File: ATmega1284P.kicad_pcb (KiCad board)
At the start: 2 copper layers, 45.7 x 22.9 mm, 23 parts, among them J1 Conn_02x03_Odd_Even, J2 Conn_01x06_Male, J3 Conn_01x17_Male, J4 Conn_01x17_Male, J5 Conn_01x01_Male, SW1 SW_Push, U1 ATmega1284P-A, Y1 16MHz

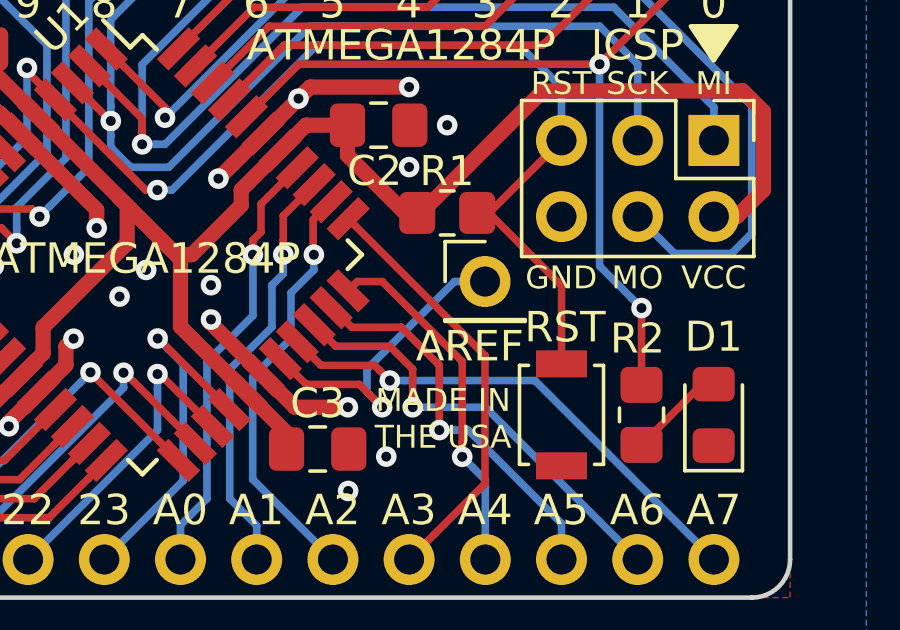
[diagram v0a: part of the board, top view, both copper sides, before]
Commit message: KiCad Files
Aligned AREF pin to be 0.1" offset from the ICSP
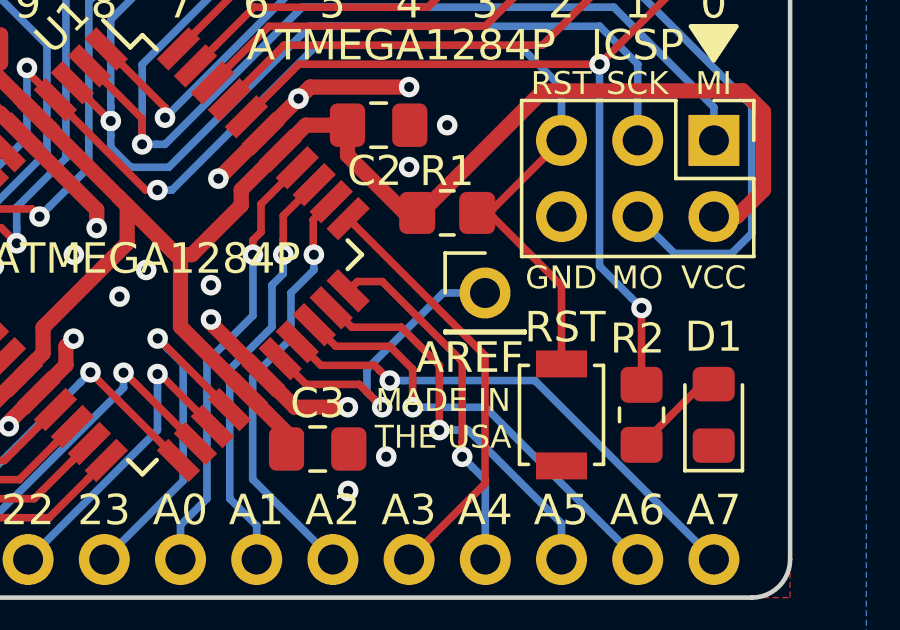
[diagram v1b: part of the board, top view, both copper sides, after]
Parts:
- moved J5 0.38 mm to (151.1, 94.4)
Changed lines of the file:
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@@
   (general
     (thickness 1.6)
-    (drawings 107)
+    (drawings 109)
     (tracks 409)
     (zones 0)
@@
   )
   (module Connector_PinHeader_2.54mm:PinHeader_1x01_P2.54mm_Vertical (layer F.Cu)
-    (at 151.13 93.98)
+    (at 151.13 94.361)
     (descr "Through hole straight pin header, 1x01, 2.54mm pitch, single row")
     (tags "Through hole pin header THT 1x01 2.54mm single row")
@@
       ))
   )
-  (gr_text AREF (at 150.622 96.139) (layer F.SilkS)
+  (gr_line (start 153.67 94.361) (end 151.13 94.361) (layer Dwgs.User) (width 0.1524))
+  (gr_line (start 153.67 91.821) (end 153.67 94.361) (layer Dwgs.User) (width 0.1524))
+  (gr_text AREF (at 150.622 96.52) (layer F.SilkS)
     (effects (font (size 1.016 1.016) (thickness 0.1524)))
   )
@@
   (segment (start 144.304926 96.550905) (end 145.163021 97.409) (width 0.254) (layer F.Cu) (net 41))
   (segment (start 145.163021 97.409) (end 146.939 97.409) (width 0.254) (layer F.Cu) (net 41))
-  (segment (start 150.114 93.98) (end 151.13 93.98) (width 0.254) (layer B.Cu) (net 41))
+  (segment (start 149.733 94.361) (end 151.13 94.361) (width 0.254) (layer B.Cu) (net 41))
+  (segment (start 147.193 96.901) (end 149.733 94.361) (width 0.254) (layer B.Cu) (net 41))
   (segment (start 147.701 98.171) (end 147.193 97.663) (width 0.254) (layer B.Cu) (net 41))
-  (segment (start 147.193 96.901) (end 150.114 93.98) (width 0.254) (layer B.Cu) (net 41))
   (segment (start 147.193 97.663) (end 147.193 96.901) (width 0.254) (layer B.Cu) (net 41))
   (zone (net 2) (net_name GND) (layer F.Cu) (hatch edge 0.508)

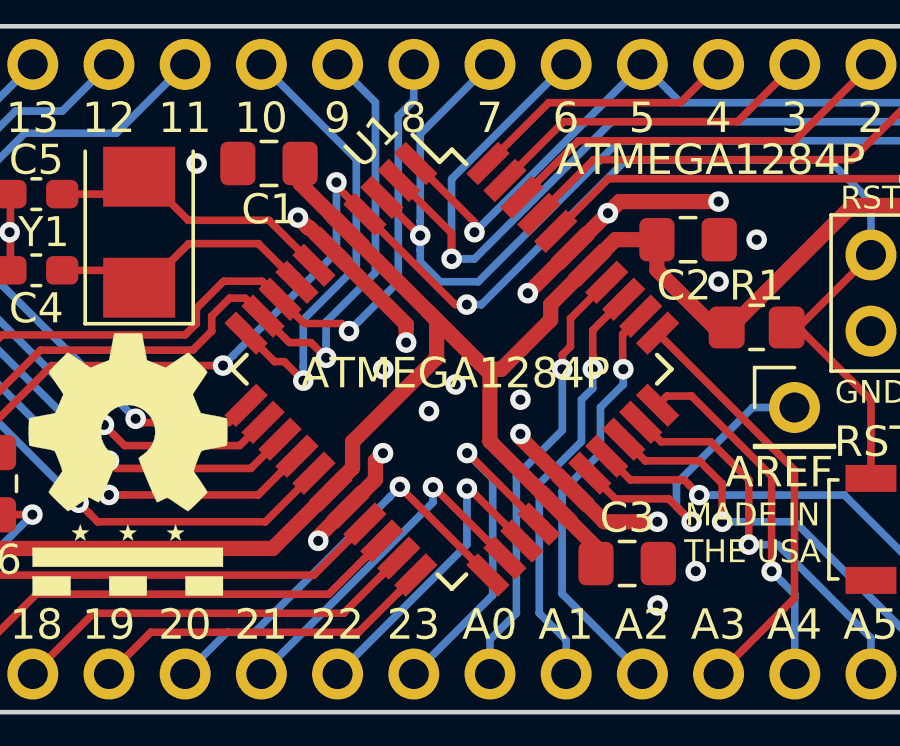
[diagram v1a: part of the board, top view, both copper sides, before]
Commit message: Added silkscreen under the ATmega1284P chip
Added the District of Columbia map shape (silkscreen) under the ATmega1284P chip.
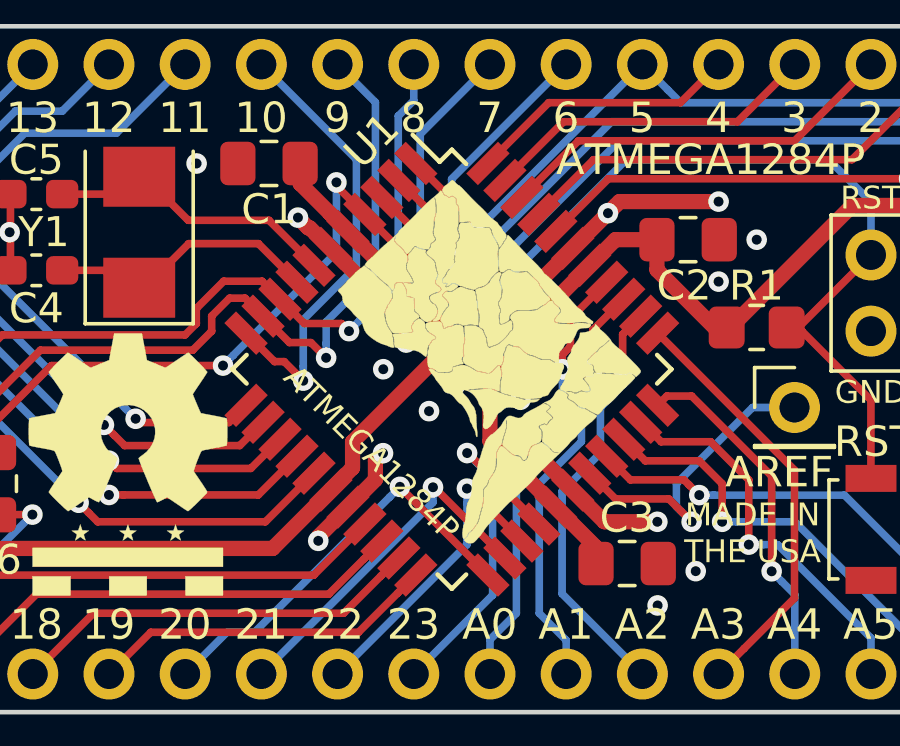
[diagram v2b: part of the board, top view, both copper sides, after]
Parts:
- added G***: LOGO, User_PCB_Libraries:DC_Diamond_small, F.Cu at (140.8, 92.8)
